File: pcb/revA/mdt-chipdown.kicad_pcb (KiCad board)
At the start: 2 copper layers, 94 x 79.6 mm, 82 parts, among them J1 SPDIF IN, J2 SPDIF OUT, J3 G3, SW1 ON_OFF, SW2 PROGRAM, U1 AMS1117-3.3, U2 Teensy4.1, U3 PCM5102A, U4 ILI9341 3.2" capacitive touch, U5 W25Q128JVS

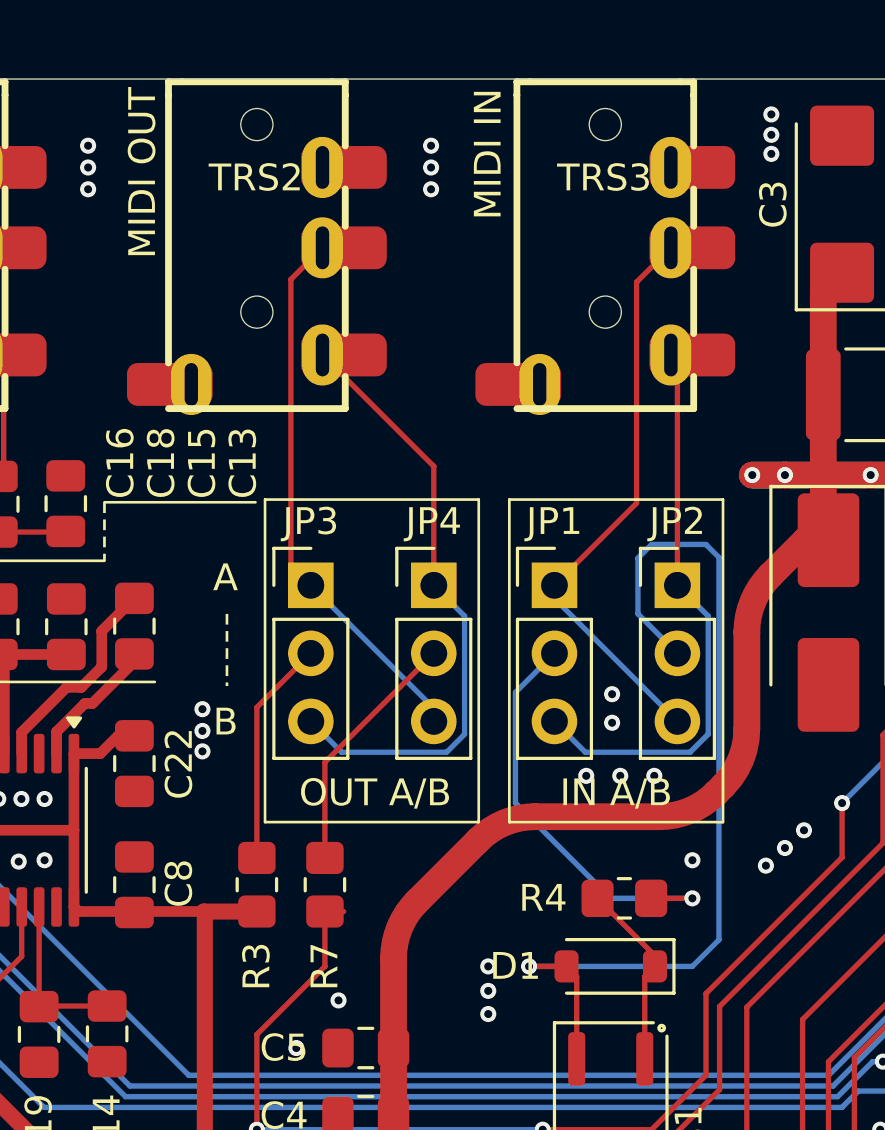
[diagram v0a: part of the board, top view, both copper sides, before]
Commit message: Updated revA: replaced jumpers with solder jumpers (preconfigured)
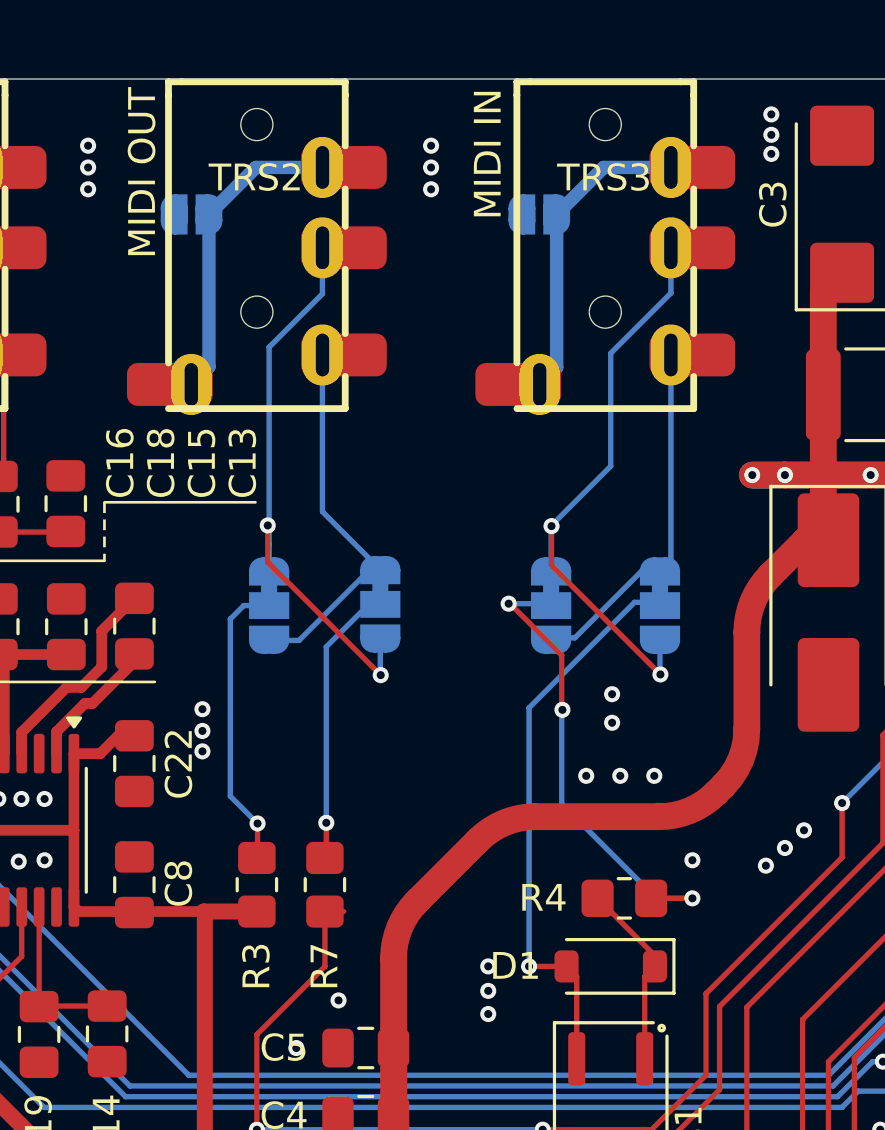
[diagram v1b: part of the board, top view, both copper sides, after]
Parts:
- added JP5: Jumper_2_Open, Jumper:SolderJumper-2_P1.3mm_Open_RoundedPad1.0x1.5mm, B.Cu at (84.2, 39.0)
- added JP6: Jumper_2_Open, Jumper:SolderJumper-2_P1.3mm_Open_RoundedPad1.0x1.5mm, B.Cu at (71.2, 39.0)
- JP1, JP2, JP3, JP4: footprint Connector_PinHeader_2.54mm:PinHeader_1x03_P2.54mm_Vertical -> Jumper:SolderJumper-3_P1.3mm_Bridged12_RoundedPad1.0x1.5mm; moved to B.Cu
- moved JP4 2.12 mm to (78.3, 53.5), turned to -90 degrees
- moved JP3 1.73 mm to (74.1, 53.6), turned to -90 degrees
- moved JP2 1.00 mm to (88.7, 53.6), turned to -90 degrees
- moved JP1 0.77 mm to (84.6, 53.6), turned to -90 degrees
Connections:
- TRS2 pad R2: GND -> Net-(JP6-A)
- TRS2 pad S: GND -> Net-(JP6-A)
- TRS3 pad R2: GND -> Net-(JP5-A)
- TRS3 pad S: GND -> Net-(JP5-A)
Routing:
- net Net-(D1-A): track 34.4 -> 21.2 mm
- net Net-(JP5-A): track 0.00 -> 11.6 mm
- net Net-(JP6-A): track 0.00 -> 11.6 mm
- net Net-(JP3-B): track 22.8 -> 14.1 mm
- net Net-(JP1-B): track 21.2 -> 13.7 mm
- net Net-(JP3-C): track 8.47 -> 11.0 mm, vias 0 -> 1
- net Net-(JP1-C): track 15.8 -> 17.7 mm, vias 1 -> 3
- net Net-(JP4-C): track 9.32 -> 10.6 mm, vias 0 -> 1
- net Net-(JP3-A): track 20.4 -> 21.6 mm, vias 0 -> 2
- net Net-(JP1-A): track 21.4 -> 22.4 mm, vias 0 -> 2
